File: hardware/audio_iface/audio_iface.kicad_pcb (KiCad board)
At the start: 2 copper layers, 4 parts, among them J401 USB_C_Receptacle_USB2.0, U201 NUCLEO_L476RG, U301 SGTL5000XNAA3, U401 USBLC6-2SC6

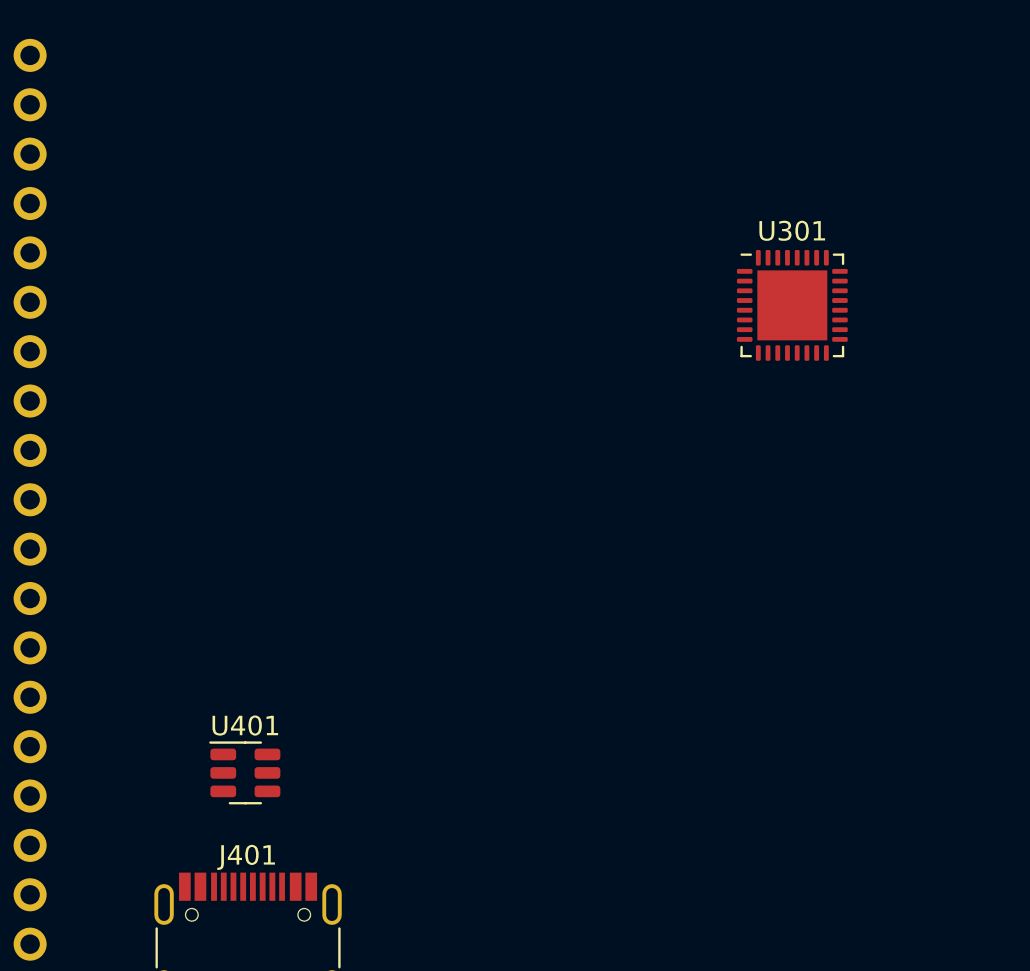
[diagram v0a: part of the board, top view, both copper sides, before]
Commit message: added some connections
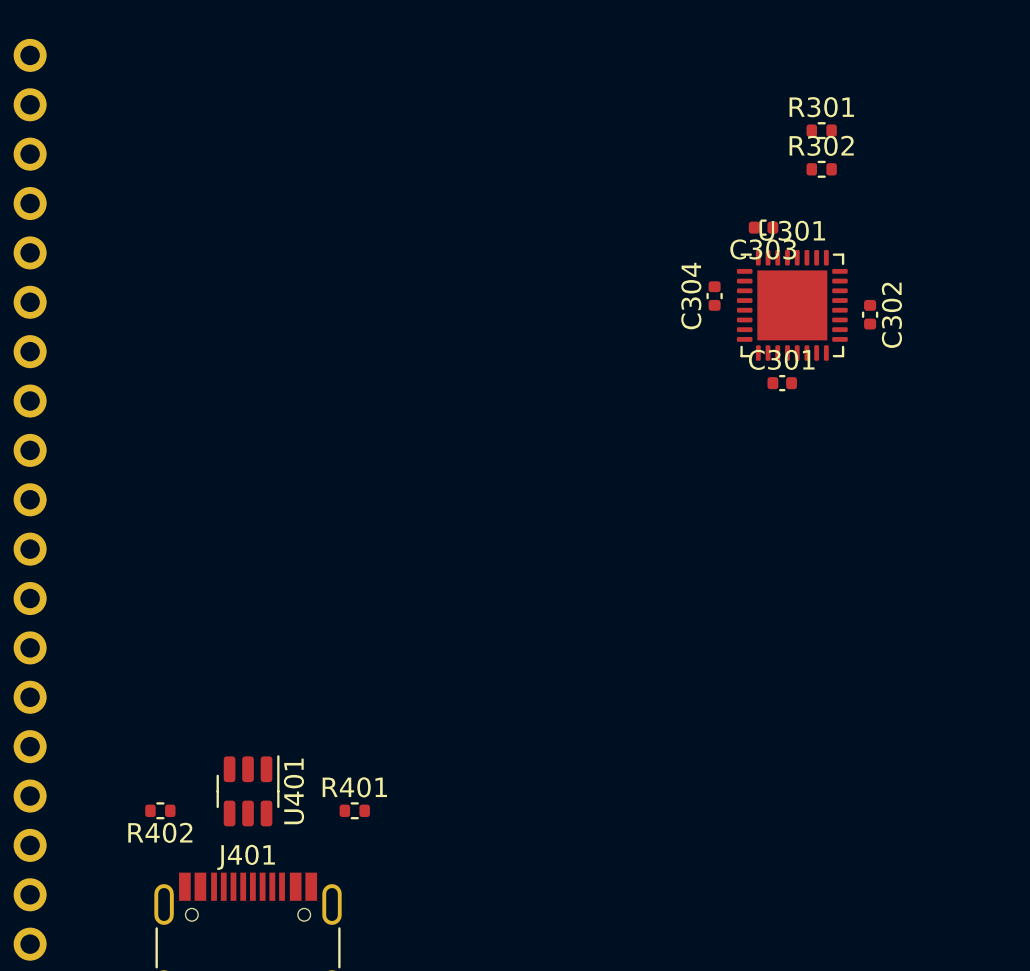
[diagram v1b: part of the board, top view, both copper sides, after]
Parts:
- added C301: 100nF, Capacitor_SMD:C_0402_1005Metric, F.Cu at (59.5, 64.0)
- added C302: 100nF, Capacitor_SMD:C_0402_1005Metric, F.Cu at (64.0, 60.5)
- added C303: 100nF, Capacitor_SMD:C_0402_1005Metric, F.Cu at (58.5, 56.0)
- added C304: 100nF, Capacitor_SMD:C_0402_1005Metric, F.Cu at (56.0, 59.5)
- added R301: 1.5k, Resistor_SMD:R_0402_1005Metric, F.Cu at (61.5, 51.0)
- added R302: 1.5k, Resistor_SMD:R_0402_1005Metric, F.Cu at (61.5, 53.0)
- added R401: 5.1k, Resistor_SMD:R_0402_1005Metric, F.Cu at (37.5, 86.0)
- added R402: 5.1k, Resistor_SMD:R_0402_1005Metric, F.Cu at (27.5, 86.0)
- moved U401 0.96 mm to (32.0, 85.0), turned to -90 degrees
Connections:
- J401 pad A1: Net-(J401-GND-PadA1) -> GND
- J401 pad A12: Net-(J401-GND-PadA1) -> GND
- J401 pad A4: Net-(J401-VBUS-PadA4) -> /USB/USBC_VBUS
- J401 pad A5: unconnected-(J401-CC1-PadA5) -> /USB/CC1
- J401 pad A6: unconnected-(J401-D+-PadA6) -> /USB/D+
- J401 pad A7: unconnected-(J401-D--PadA7) -> /USB/D-
- J401 pad A9: Net-(J401-VBUS-PadA4) -> /USB/USBC_VBUS
- J401 pad B1: Net-(J401-GND-PadA1) -> GND
- J401 pad B12: Net-(J401-GND-PadA1) -> GND
- J401 pad B4: Net-(J401-VBUS-PadA4) -> /USB/USBC_VBUS
- J401 pad B5: unconnected-(J401-CC2-PadB5) -> /USB/CC2
- J401 pad B6: unconnected-(J401-D+-PadB6) -> /USB/D+
- J401 pad B7: unconnected-(J401-D--PadB7) -> /USB/D-
- J401 pad B9: Net-(J401-VBUS-PadA4) -> /USB/USBC_VBUS
- U201 pad 108: unconnected-(U201A-GND-Pad108) -> GND
- U201 pad 119: unconnected-(U201A-GND-Pad119) -> GND
- U201 pad 120: unconnected-(U201A-GND-Pad120) -> GND
- U201 pad 122: unconnected-(U201A-GND-Pad122) -> GND
- U201 pad 209: unconnected-(U201A-GND-Pad209) -> GND
- U201 pad 220: unconnected-(U201A-GND-Pad220) -> GND
- U201 pad 232: unconnected-(U201A-AGND-Pad232) -> GND
- U301 pad 1: Net-(U301-GND-Pad1) -> GND
- U301 pad 10: unconnected-(U301-VAG-Pad10) -> /AUDIO CODEC/VAG
- U301 pad 13: unconnected-(U301-LINEIN_R-Pad13) -> /AUDIO CODEC/LINEIN_R
- U301 pad 14: unconnected-(U301-LINEIN_L-Pad14) -> /AUDIO CODEC/LINEIN_L
- U301 pad 2: unconnected-(U301-HP_R-Pad2) -> /AUDIO CODEC/HP_R
- U301 pad 20: unconnected-(U301-VDDIO-Pad20) -> +3V3
- U301 pad 21: unconnected-(U301-SYS_MCLK-Pad21) -> /AUDIO CODEC/SYS_MCLK
- U301 pad 23: unconnected-(U301-I2S_LRCLK-Pad23) -> /AUDIO CODEC/I2S_LRCLK
- U301 pad 24: unconnected-(U301-I2S_SCLK-Pad24) -> /AUDIO CODEC/I2S_SCLK
- U301 pad 25: unconnected-(U301-I2S_DOUT-Pad25) -> /AUDIO CODEC/I2S_DOUT
- U301 pad 26: unconnected-(U301-I2S_DIN-Pad26) -> /AUDIO CODEC/I2S_DIN
- U301 pad 27: unconnected-(U301-CTRL_DATA-Pad27) -> /AUDIO CODEC/I2C_SDA
- U301 pad 29: unconnected-(U301-CTRL_CLK-Pad29) -> /AUDIO CODEC/I2C_SCL
- U301 pad 3: Net-(U301-GND-Pad1) -> GND
- U301 pad 30: unconnected-(U301-VDDD-Pad30) -> +1V8
- U301 pad 31: unconnected-(U301-CTRL_ADR0_CS-Pad31) -> GND
- U301 pad 32: unconnected-(U301-CTRL_MODE-Pad32) -> GND
- U301 pad 33: Net-(U301-GND-Pad1) -> GND
- U301 pad 4: unconnected-(U301-HP_VGND-Pad4) -> /AUDIO CODEC/HP_VGND
- U301 pad 5: unconnected-(U301-VDDA-Pad5) -> +3.3VA
- U301 pad 6: unconnected-(U301-HP_L-Pad6) -> /AUDIO CODEC/HP_L
- U301 pad 7: unconnected-(U301-AGND-Pad7) -> GND
- U401 pad 1: unconnected-(U401-I/O1-Pad1) -> /NUCLEO/USB_D+
- U401 pad 2: unconnected-(U401-GND-Pad2) -> GND
- U401 pad 3: unconnected-(U401-I/O2-Pad3) -> /NUCLEO/USB_D-
- U401 pad 4: unconnected-(U401-I/O2-Pad4) -> /USB/D-
- U401 pad 5: unconnected-(U401-VBUS-Pad5) -> /USB/USBC_VBUS
- U401 pad 6: unconnected-(U401-I/O1-Pad6) -> /USB/D+

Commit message: schematic v1 done
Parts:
- added C305: 1uF, Capacitor_SMD:C_0603_1608Metric, F.Cu at (44.8, 17.6)
- added C306: 1uF, Capacitor_SMD:C_0603_1608Metric, F.Cu at (44.8, 20.1)
- added C307: 1uF, Capacitor_SMD:C_0603_1608Metric, F.Cu at (44.8, 22.6)
- added C308: 1uF, Capacitor_SMD:C_0603_1608Metric, F.Cu at (44.8, 25.2)
- added C309: 1uF, Capacitor_SMD:C_0603_1608Metric, F.Cu at (44.8, 27.7)
- added C310: 100nF, Capacitor_SMD:C_0402_1005Metric, F.Cu at (44.3, 31.9)
- added C501: 100nF, Capacitor_SMD:C_0402_1005Metric, F.Cu at (50.3, 36.8)
- added D501: GREEN, LED_SMD:LED_0603_1608Metric, F.Cu at (63.8, 17.7)
- added D502: GREEN, LED_SMD:LED_0603_1608Metric, F.Cu at (63.8, 20.3)
- added D503: GREEN, LED_SMD:LED_0603_1608Metric, F.Cu at (63.8, 22.9)
- added D504: GREEN, LED_SMD:LED_0603_1608Metric, F.Cu at (63.8, 25.4)
- added D505: GREEN, LED_SMD:LED_0603_1608Metric, F.Cu at (63.8, 28.0)
- added D506: ORANGE, LED_SMD:LED_0603_1608Metric, F.Cu at (63.8, 30.6)
- added D507: ORANGE, LED_SMD:LED_0603_1608Metric, F.Cu at (67.8, 17.7)
- added D508: RED, LED_SMD:LED_0603_1608Metric, F.Cu at (67.8, 20.3)
- added D509: GREEN, LED_SMD:LED_0603_1608Metric, F.Cu at (67.8, 22.9)
- added D510: GREEN, LED_SMD:LED_0603_1608Metric, F.Cu at (67.8, 25.4)
- added D511: GREEN, LED_SMD:LED_0603_1608Metric, F.Cu at (67.8, 28.0)
- added D512: GREEN, LED_SMD:LED_0603_1608Metric, F.Cu at (67.8, 30.6)
- added D513: GREEN, LED_SMD:LED_0603_1608Metric, F.Cu at (71.9, 17.7)
- added D514: ORANGE, LED_SMD:LED_0603_1608Metric, F.Cu at (71.9, 20.3)
- added D515: ORANGE, LED_SMD:LED_0603_1608Metric, F.Cu at (71.9, 22.9)
- added D516: RED, LED_SMD:LED_0603_1608Metric, F.Cu at (71.9, 25.4)
- added J201: UART, Connector_JST:JST_XH_S3B-XH-A_1x03_P2.50mm_Horizontal, F.Cu at (58.5, 88.0)
- added J301: AudioJack4, Connector_Audio:Jack_3.5mm_PJ320D_Horizontal, F.Cu at (36.2, 21.9)
- added J302: AudioJack4, Connector_Audio:Jack_3.5mm_PJ320D_Horizontal, F.Cu at (36.2, 33.0)
- added J303: AudioJack4, Connector_Audio:Jack_3.5mm_PJ320D_Horizontal, F.Cu at (36.2, 44.0)
- added MK301: Microphone, WITNS:Electret_ABM-713-RC, F.Cu at (37.1, 62.0)
- added R303: 5.1k, Resistor_SMD:R_0402_1005Metric, F.Cu at (44.3, 29.9)
- added R501: R_Small, Resistor_SMD:R_0603_1608Metric, F.Cu at (63.7, 33.2)
- added R502: R_Small, Resistor_SMD:R_0603_1608Metric, F.Cu at (63.7, 35.7)
- added R503: R_Small, Resistor_SMD:R_0603_1608Metric, F.Cu at (63.7, 38.2)
- added R504: R_Small, Resistor_SMD:R_0603_1608Metric, F.Cu at (63.7, 40.7)
- added R505: R_Small, Resistor_SMD:R_0603_1608Metric, F.Cu at (63.7, 43.2)
- added R506: R_Small, Resistor_SMD:R_0603_1608Metric, F.Cu at (63.7, 45.7)
- added R507: R_Small, Resistor_SMD:R_0603_1608Metric, F.Cu at (67.8, 33.2)
- added R508: R_Small, Resistor_SMD:R_0603_1608Metric, F.Cu at (67.8, 35.7)
- added R509: R_Small, Resistor_SMD:R_0603_1608Metric, F.Cu at (67.8, 38.2)
- added R510: R_Small, Resistor_SMD:R_0603_1608Metric, F.Cu at (67.8, 40.7)
- added R511: R_Small, Resistor_SMD:R_0603_1608Metric, F.Cu at (67.8, 43.2)
- added R512: R_Small, Resistor_SMD:R_0603_1608Metric, F.Cu at (67.8, 45.7)
- added R513: R_Small, Resistor_SMD:R_0603_1608Metric, F.Cu at (71.8, 33.2)
- added R514: R_Small, Resistor_SMD:R_0603_1608Metric, F.Cu at (71.8, 35.7)
- added R515: R_Small, Resistor_SMD:R_0603_1608Metric, F.Cu at (71.8, 38.2)
- added R516: R_Small, Resistor_SMD:R_0603_1608Metric, F.Cu at (71.8, 40.7)
- added TP101: TestPoint, Connector_Pin:Pin_D1.1mm_L8.5mm_W2.5mm_FlatFork, F.Cu at (110.8, 24.5)
- added TP102: TestPoint, Connector_Pin:Pin_D1.1mm_L8.5mm_W2.5mm_FlatFork, F.Cu at (110.8, 28.8)
- added TP103: TestPoint, Connector_Pin:Pin_D1.1mm_L8.5mm_W2.5mm_FlatFork, F.Cu at (110.8, 33.0)
- added TP104: TestPoint, Connector_Pin:Pin_D1.1mm_L8.5mm_W2.5mm_FlatFork, F.Cu at (115.4, 24.5)
- added TP105: TestPoint, Connector_Pin:Pin_D1.1mm_L8.5mm_W2.5mm_FlatFork, F.Cu at (115.4, 28.8)
- added TP106: TestPoint, Connector_Pin:Pin_D1.1mm_L8.5mm_W2.5mm_FlatFork, F.Cu at (115.4, 33.0)
- added TP107: TestPoint, Connector_Pin:Pin_D1.1mm_L8.5mm_W2.5mm_FlatFork, F.Cu at (119.9, 24.5)
- added TP108: TestPoint, Connector_Pin:Pin_D1.1mm_L8.5mm_W2.5mm_FlatFork, F.Cu at (119.9, 28.8)
- added TP109: TestPoint, Connector_Pin:Pin_D1.1mm_L8.5mm_W2.5mm_FlatFork, F.Cu at (119.9, 33.0)
- added TP110: TestPoint, Connector_Pin:Pin_D1.1mm_L8.5mm_W2.5mm_FlatFork, F.Cu at (124.5, 24.5)
- added TP111: TestPoint, Connector_Pin:Pin_D1.1mm_L8.5mm_W2.5mm_FlatFork, F.Cu at (124.5, 28.8)
- added TP112: TestPoint, Connector_Pin:Pin_D1.1mm_L8.5mm_W2.5mm_FlatFork, F.Cu at (124.5, 33.0)
- added TP201: TestPoint, Connector_Pin:Pin_D1.1mm_L8.5mm_W2.5mm_FlatFork, F.Cu at (104.3, 24.5)
- added TP202: TestPoint, Connector_Pin:Pin_D1.1mm_L8.5mm_W2.5mm_FlatFork, F.Cu at (104.3, 28.8)
- added TP203: TestPoint, Connector_Pin:Pin_D1.1mm_L8.5mm_W2.5mm_FlatFork, F.Cu at (104.3, 33.0)
- added TP204: TestPoint, Connector_Pin:Pin_D1.1mm_L8.5mm_W2.5mm_FlatFork, F.Cu at (104.3, 37.3)
- added TP301: TestPoint, Connector_Pin:Pin_D1.1mm_L8.5mm_W2.5mm_FlatFork, F.Cu at (97.7, 24.5)
- added TP302: TestPoint, Connector_Pin:Pin_D1.1mm_L8.5mm_W2.5mm_FlatFork, F.Cu at (97.7, 28.8)
- added TP303: TestPoint, Connector_Pin:Pin_D1.1mm_L8.5mm_W2.5mm_FlatFork, F.Cu at (97.7, 33.0)
- added TP304: TestPoint, Connector_Pin:Pin_D1.1mm_L8.5mm_W2.5mm_FlatFork, F.Cu at (97.7, 37.3)
- added TP305: TestPoint, Connector_Pin:Pin_D1.1mm_L8.5mm_W2.5mm_FlatFork, F.Cu at (97.7, 41.5)
- added U501: MCP23S17-E/SO, Package_SO:SOIC-28W_7.5x17.9mm_P1.27mm, F.Cu at (55.3, 26.1)
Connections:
- U201 pad 105: unconnected-(U201A-VDD-Pad105) -> +3.3V
- U201 pad 207: unconnected-(U201A-AVDD-Pad207) -> +3.3VA
- U201 pad 212: unconnected-(U201B-PA12-Pad212) -> /NUCLEO/USB_D+
- U201 pad 214: unconnected-(U201B-PA11-Pad214) -> /NUCLEO/USB_D-
- U301 pad 11: unconnected-(U301-LINEOUT_R-Pad11) -> /AUDIO CODEC/LINEOUT_R
- U301 pad 12: unconnected-(U301-LINEOUT_L-Pad12) -> /AUDIO CODEC/LINEOUT_L
- U301 pad 15: unconnected-(U301-MIC-Pad15) -> Net-(U301-MIC)
- U301 pad 16: unconnected-(U301-MIC_BIAS-Pad16) -> Net-(U301-MIC_BIAS)

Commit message: crude placement
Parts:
- TP101: value TestPoint -> MCLK
- TP102: value TestPoint -> SCLK
- TP103: value TestPoint -> LRCLK
- TP104: value TestPoint -> DIN
- TP105: value TestPoint -> DOUT
- TP106: value TestPoint -> SCL
- TP107: value TestPoint -> SDA
- TP108: value TestPoint -> nRESET
- TP109: value TestPoint -> MISO
- TP110: value TestPoint -> MOSI
- TP111: value TestPoint -> SCK
- TP112: value TestPoint -> nCS
- TP201: value TestPoint -> +3.3V
- TP202: value TestPoint -> +3.3VA
- TP203: value TestPoint -> RX
- TP204: value TestPoint -> TX
- moved TP302 92.6 mm to (32.0, 94.0)
- moved TP301 92.5 mm to (27.4, 84.5)
- moved TP111 88.1 mm to (40.6, 55.9)
- moved TP108 86.1 mm to (40.0, 60.7)
- moved TP303 86.0 mm to (37.0, 94.0)
- moved TP112 85.6 mm to (40.8, 51.2)
- moved C306 82.9 mm to (44.0, 103.0), turned to -90 degrees
- moved J301 81.6 mm to (35.0, 103.5), turned to 90 degrees
- moved C305 81.4 mm to (44.0, 99.0), turned to -90 degrees
- moved TP201 79.5 mm to (29.4, 51.2)
- moved TP202 79.5 mm to (29.4, 55.5)
- moved C308 79.4 mm to (29.0, 103.0), turned to 90 degrees
- moved C307 78.0 mm to (29.0, 99.0), turned to 90 degrees
- moved TP101 76.4 mm to (58.1, 79.9)
- moved TP102 76.4 mm to (58.1, 84.2)
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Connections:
- net Net-(D501-K) renamed /VU METER/GPB0
- net Net-(D502-K) renamed /VU METER/GPB1
- net Net-(D503-K) renamed /VU METER/GPB2
- net Net-(D504-K) renamed /VU METER/GPB3
- net Net-(D505-K) renamed /VU METER/GPB4
- net Net-(D506-K) renamed /VU METER/GPB5
- net Net-(D507-K) renamed /VU METER/GPB6
- net Net-(D508-K) renamed /VU METER/GPB7
- net Net-(D509-K) renamed /VU METER/GPA0
- net Net-(D510-K) renamed /VU METER/GPA1
- net Net-(D511-K) renamed /VU METER/GPA2
- net Net-(D512-K) renamed /VU METER/GPA3
- net Net-(D513-K) renamed /VU METER/GPA4
- net Net-(D514-K) renamed /VU METER/GPA5
- net Net-(D515-K) renamed /VU METER/GPA6
- net Net-(D516-K) renamed /VU METER/GPA7
- U201 pad 101: unconnected-(U201B-PC10-Pad101) -> /NUCLEO/VU_SCK
- U201 pad 102: unconnected-(U201B-PC11-Pad102) -> /NUCLEO/VU_MISO
- U201 pad 103: unconnected-(U201B-PC12-Pad103) -> /AUDIO CODEC/I2S_DOUT
- U201 pad 121: unconnected-(U201B-PB7-Pad121) -> /NUCLEO/VU_nRESET
- U201 pad 216: unconnected-(U201B-PB12-Pad216) -> /AUDIO CODEC/I2S_LRCLK
- U201 pad 217: unconnected-(U201B-PB6-Pad217) -> /NUCLEO/VU_nCS
- U201 pad 218: unconnected-(U201B-PB11-Pad218) -> /AUDIO CODEC/I2C_SDA
- U201 pad 221: unconnected-(U201B-PA9-Pad221) -> /NUCLEO/UART_TX
- U201 pad 225: unconnected-(U201B-PB10-Pad225) -> /AUDIO CODEC/I2C_SCL
- U201 pad 226: unconnected-(U201B-PB15-Pad226) -> /AUDIO CODEC/I2S_DIN
- U201 pad 228: unconnected-(U201B-PB14-Pad228) -> /AUDIO CODEC/SYS_MCLK
- U201 pad 229: unconnected-(U201B-PB5-Pad229) -> /NUCLEO/VU_MOSI
- U201 pad 230: unconnected-(U201B-PB13-Pad230) -> /AUDIO CODEC/I2S_SCLK
- U201 pad 233: unconnected-(U201B-PA10-Pad233) -> /NUCLEO/UART_RX
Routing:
- net /VU METER/GPA7: track 0.00 -> 52.0 mm
- net /VU METER/GPA6: track 0.00 -> 49.2 mm
- net /VU METER/GPA5: track 0.00 -> 46.9 mm
- net /VU METER/GPA4: track 0.00 -> 44.7 mm
- net /VU METER/GPA3: track 0.00 -> 42.3 mm
- net /VU METER/GPA2: track 0.00 -> 39.5 mm
- net /VU METER/GPA1: track 0.00 -> 36.6 mm
- net /VU METER/GPA0: track 0.00 -> 33.4 mm
- net /VU METER/GPB7: track 0.00 -> 8.64 mm
- net /VU METER/GPB6: track 0.00 -> 7.58 mm
- net /VU METER/GPB5: track 0.00 -> 6.52 mm
- net /VU METER/GPB4: track 0.00 -> 5.88 mm
- net /VU METER/GPB3: track 0.00 -> 5.58 mm
- net /VU METER/GPB2: track 0.00 -> 5.27 mm
- net /VU METER/GPB1: track 0.00 -> 4.97 mm
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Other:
- board outline added: 70 x 66 mm

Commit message: routing v1
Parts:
- added TP205: GND, Connector_Pin:Pin_D1.1mm_L8.5mm_W2.5mm_FlatFork, F.Cu at (69.5, 75.3)
- added TP306: R, Connector_Pin:Pin_D1.1mm_L8.5mm_W2.5mm_FlatFork, F.Cu at (32.0, 94.0)
- added TP307: HP GND, Connector_Pin:Pin_D1.1mm_L8.5mm_W2.5mm_FlatFork, F.Cu at (42.0, 94.0)
- added TP308: L, Connector_Pin:Pin_D1.1mm_L8.5mm_W2.5mm_FlatFork, F.Cu at (37.0, 94.0)
- J301: value AudioJack4 -> LINEIN
- J302: value AudioJack4 -> HP
- J303: value AudioJack4 -> LINEOUT
- TP301: value TestPoint -> MIC
- TP302, TP304: value TestPoint -> R
- TP303, TP305: value TestPoint -> L
- moved J401 62.0 mm to (81.0, 103.0), turned to 90 degrees
- moved R402 57.9 mm to (79.5, 109.0)
- moved R401 57.7 mm to (79.5, 97.0)
- moved J201 51.8 mm to (24.4, 100.5), turned to -90 degrees
- moved U401 47.4 mm to (73.0, 100.0)
- moved TP204 47.4 mm to (26.0, 89.0), turned to 180 degrees
- moved TP203 47.4 mm to (26.0, 94.0), turned to 180 degrees
- moved TP202 44.8 mm to (74.0, 51.0)
- moved TP107 36.2 mm to (31.0, 80.0)
- moved TP105 36.0 mm to (30.0, 69.0)
- moved TP104 33.2 mm to (30.0, 74.0)
- moved TP106 31.9 mm to (31.0, 85.0)
- moved C307 30.0 mm to (59.0, 99.0)
- moved C308 30.0 mm to (59.0, 103.0)
- moved J301 30.0 mm to (65.0, 103.5)
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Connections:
- net Net-(U301-MIC) renamed /AUDIO CODEC/MIC
- net Net-(U301-MIC_BIAS) renamed /AUDIO CODEC/MIC_BIAS
- C302 pad 1: +3V3 -> +3.3V
- R301 pad 1: +3V3 -> +3.3V
- R302 pad 1: +3V3 -> +3.3V
- U201 pad 121: /NUCLEO/VU_nRESET -> /NUCLEO/VU_nCS
- U201 pad 128: unconnected-(U201B-PA0-Pad128) -> /NUCLEO/VU_nRESET
- U201 pad 217: /NUCLEO/VU_nCS -> unconnected-(U201B-PB6-Pad217)
- U301 pad 20: +3V3 -> +3.3V
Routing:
- net +3.3V: track 2.30 -> 140.5 mm, vias 0 -> 6
- net /NUCLEO/UART_TX: track 0.00 -> 111.2 mm
- net +3.3VA: track 0.00 -> 99.1 mm, vias 0 -> 3
- net /AUDIO CODEC/I2C_SCL: track 0.00 -> 79.6 mm
- net /NUCLEO/UART_RX: track 0.00 -> 74.4 mm
- net /AUDIO CODEC/I2C_SDA: track 0.00 -> 73.3 mm
- net /AUDIO CODEC/I2S_DIN: track 0.00 -> 67.3 mm
- net /NUCLEO/VU_MOSI: track 0.00 -> 63.4 mm
- net /NUCLEO/VU_nCS: track 0.00 -> 56.4 mm, vias 0 -> 1
- net /AUDIO CODEC/I2S_LRCLK: track 0.00 -> 55.6 mm
- net /AUDIO CODEC/I2S_SCLK: track 0.00 -> 53.1 mm, vias 0 -> 1
- net /NUCLEO/USB_D-: track 0.00 -> 51.9 mm
- net /AUDIO CODEC/SYS_MCLK: track 0.00 -> 51.2 mm
- net /NUCLEO/VU_MISO: track 0.00 -> 49.1 mm
- net /NUCLEO/VU_SCK: track 0.00 -> 47.2 mm
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- added copper zone on B.Cu, net GND
- added copper zone on F.Cu, net GND
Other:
- outline, holes or cut-outs redrawn
